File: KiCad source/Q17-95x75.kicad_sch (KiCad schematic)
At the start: 78 parts, among them J1 Input, J2 Terminal, J3 Terminal, Q1 IRF610, Q10 2SA970, Q11 BS250P, Q12 2SC2240 / AC181, Q13 IRF610, Q14 IRF9610, Q15 FQA46N15, Q16 FQA36P15, Q2 2SA970, Q3 2SC2240, Q4 IRF9610, Q5 IRF9610, Q6 IRF610, Q7 2SC2240, Q8 2N7000, Q9 BS250P, U1 OPA1641

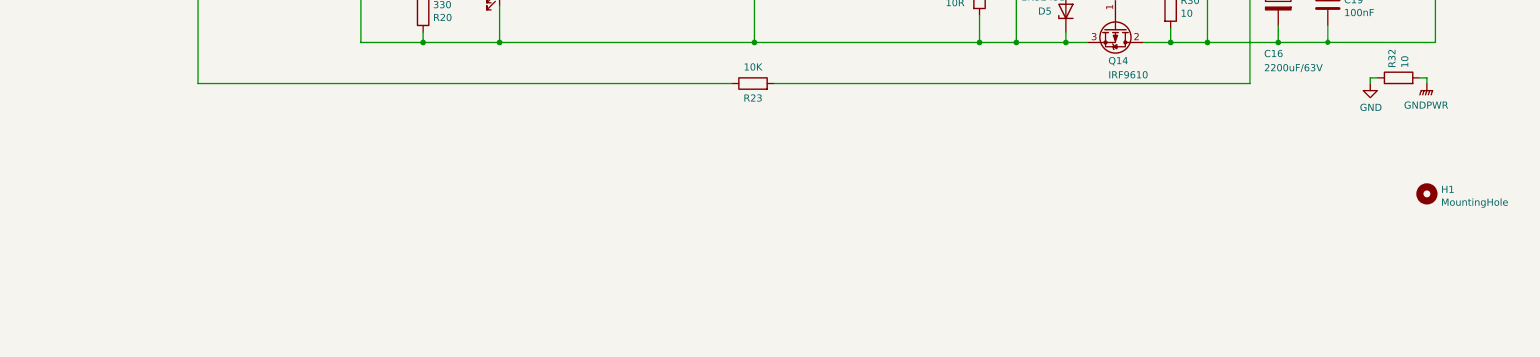
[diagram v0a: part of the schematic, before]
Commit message: General cleanup and parts references added in schematic.
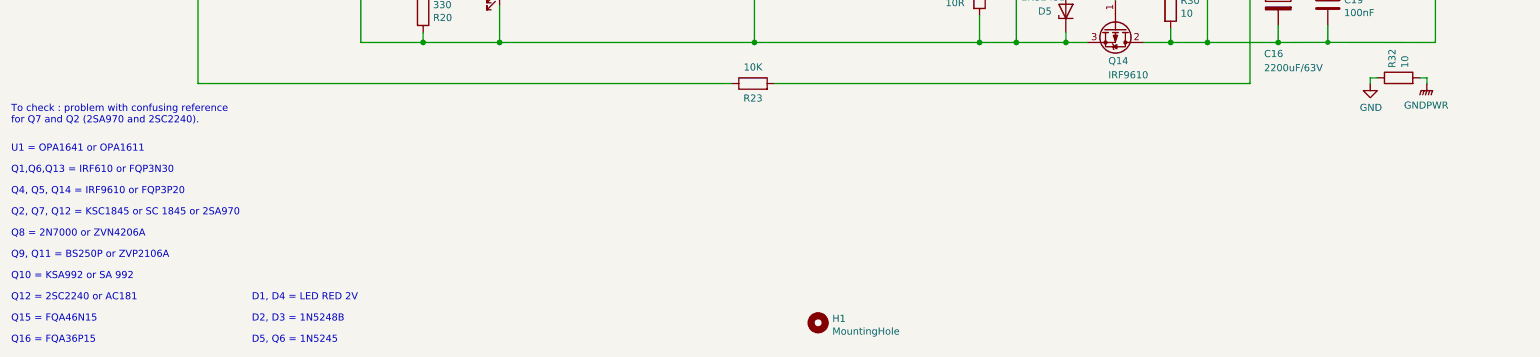
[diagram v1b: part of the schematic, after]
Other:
- note added: "D1, D4 = LED RED 2V"
- note added: "D2, D3 = 1N5248B"
- note added: "D5, Q6 = 1N5245"
- note added: "Q1,Q6,Q13 = IRF610 or FQP3N30"
- note added: "Q10 = KSA992 or SA 992"
- note added: "Q12 = 2SC2240 or AC181"
- note added: "Q15 = FQA46N15"
- note added: "Q16 = FQA36P15"
- note added: "Q2, Q7, Q12 = KSC1845 or SC 1845 or 2SA970"
- note added: "Q4, Q5, Q14 = IRF9610 or FQP3P20"
- note added: "Q8 = 2N7000 or ZVN4206A"
- note added: "Q9, Q11 = BS250P or ZVP2106A"
- note added: "To check : problem with confusing reference for Q7 and Q2 (2SA970 and 2SC2240)."
- note added: "U1 = OPA1641 or OPA1611"
- title: Q17 -> Q17 Amplifier
- moved on the sheet: H1

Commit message: Update diagram for Q17-95x75
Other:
- note added: "C1 and C7 : Use good MKP capacitor."
- note added: "C10 : Use good Mica cacaitor."
- note added: "C6 : Use bipolar capacitor if possible."
- note added: "D1, D4 : LED RED 2V"
- note added: "D2, D3 : 1N5248B"
- note added: "D5, Q6 : 1N5245"
- note added: "L1 : Use 18 turns of 1mm copper insulated wire with a 8mm diameter tube."
- note added: "Q1, Q6, Q13 : IRF610 or FQP3N30"
- note added: "Q10 : KSA992"
- note added: "Q12 : 2SC2240 or AC181"
- note added: "Q15 : FQA46N15"
- note added: "Q16 : FQA36P15"
- note added: "Q2, Q7, Q12 : KSC1845 or 2SA970"
- note added: "Q4, Q5, Q14 : IRF9610 or FQP3P20"
- note added: "Q8 : 2N7000 or ZVN4206AV"
- note added: "Q9, Q11 : BS250P (Diodes Inc) or ZVP2106A"
- note added: "U1 : OPA1641 or OPA1611"
- note removed: "D1, D4 = LED RED 2V"
- note removed: "D2, D3 = 1N5248B"
- note removed: "D5, Q6 = 1N5245"
- note removed: "Q1,Q6,Q13 = IRF610 or FQP3N30"
- note removed: "Q10 = KSA992 or SA 992"
- note removed: "Q12 = 2SC2240 or AC181"
- note removed: "Q15 = FQA46N15"
- note removed: "Q16 = FQA36P15"
- note removed: "Q2, Q7, Q12 = KSC1845 or SC 1845 or 2SA970"
- note removed: "Q4, Q5, Q14 = IRF9610 or FQP3P20"
- note removed: "Q8 = 2N7000 or ZVN4206A"
- note removed: "Q9, Q11 = BS250P or ZVP2106A"
- note removed: "To check : problem with confusing reference for Q7 and Q2 (2SA970 and 2SC2240)."
- note removed: "U1 = OPA1641 or OPA1611"

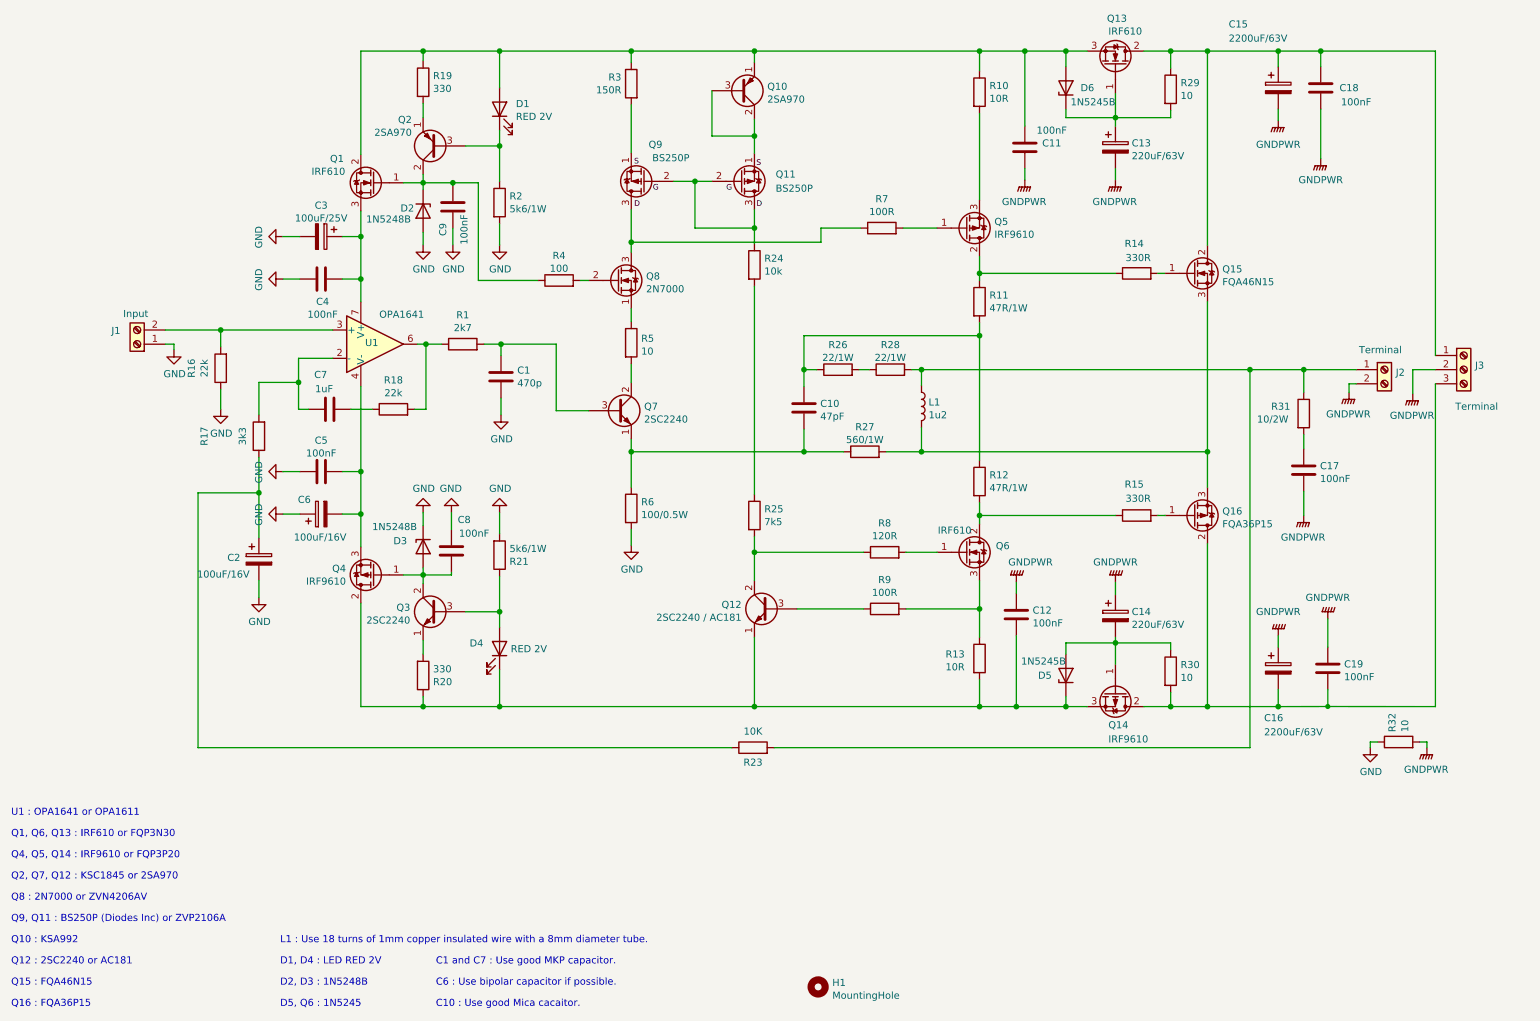
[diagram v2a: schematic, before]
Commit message: Update PCB to 10b12
- Changed footprint for KSC1845 (Q2, Q7 and Q12).
- Updated transistors references on diagram and PCB.
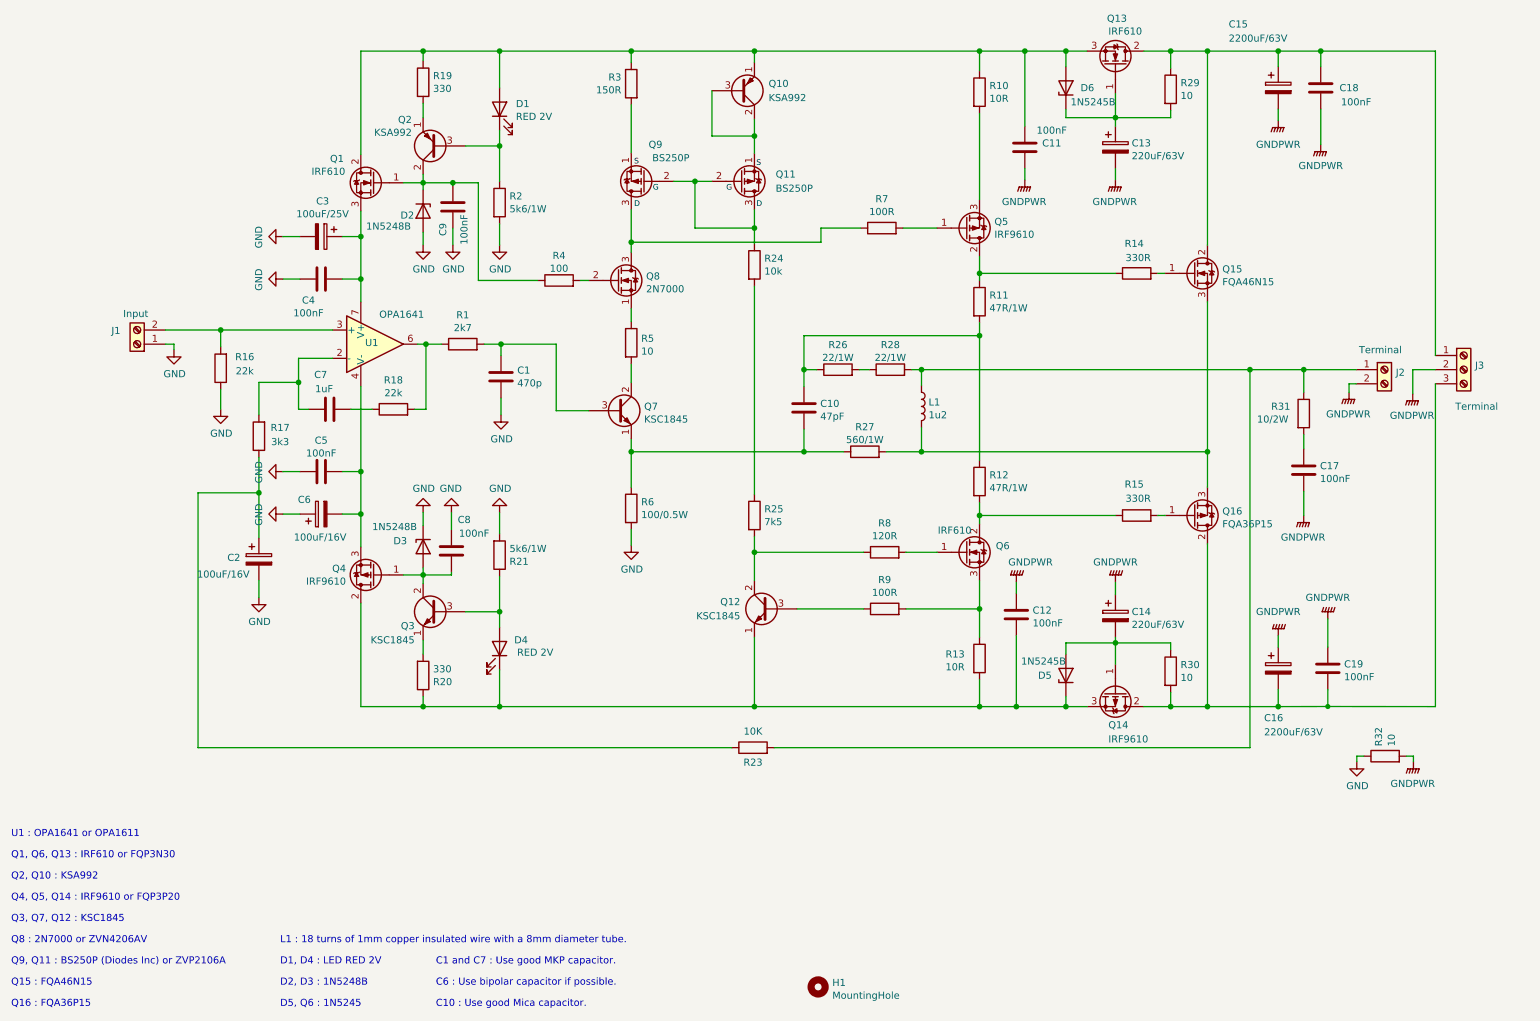
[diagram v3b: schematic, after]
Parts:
- Q10, Q2: value 2SA970 -> KSA992
- Q12: value 2SC2240 / AC181 -> KSC1845
- Q3, Q7: value 2SC2240 -> KSC1845
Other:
- note added: "C10 : Use good Mica capacitor."
- note added: "L1 : 18 turns of 1mm copper insulated wire with a 8mm diameter tube."
- note added: "Q2, Q10 : KSA992"
- note added: "Q3, Q7, Q12 : KSC1845"
- note removed: "C10 : Use good Mica cacaitor."
- note removed: "L1 : Use 18 turns of 1mm copper insulated wire with a 8mm diameter tube."
- note removed: "Q10 : KSA992"
- note removed: "Q12 : 2SC2240 or AC181"
- note removed: "Q2, Q7, Q12 : KSC1845 or 2SA970"
- moved on the sheet: R32

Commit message: Update Diagram and PCB to 1.0b13
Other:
- note added: "C1 and C10 : Use good Mica or Polystyrene capacitor."
- note added: "C7 : Use good MKP capacitor."
- note removed: "C1 and C7 : Use good MKP capacitor."
- note removed: "C10 : Use good Mica capacitor."

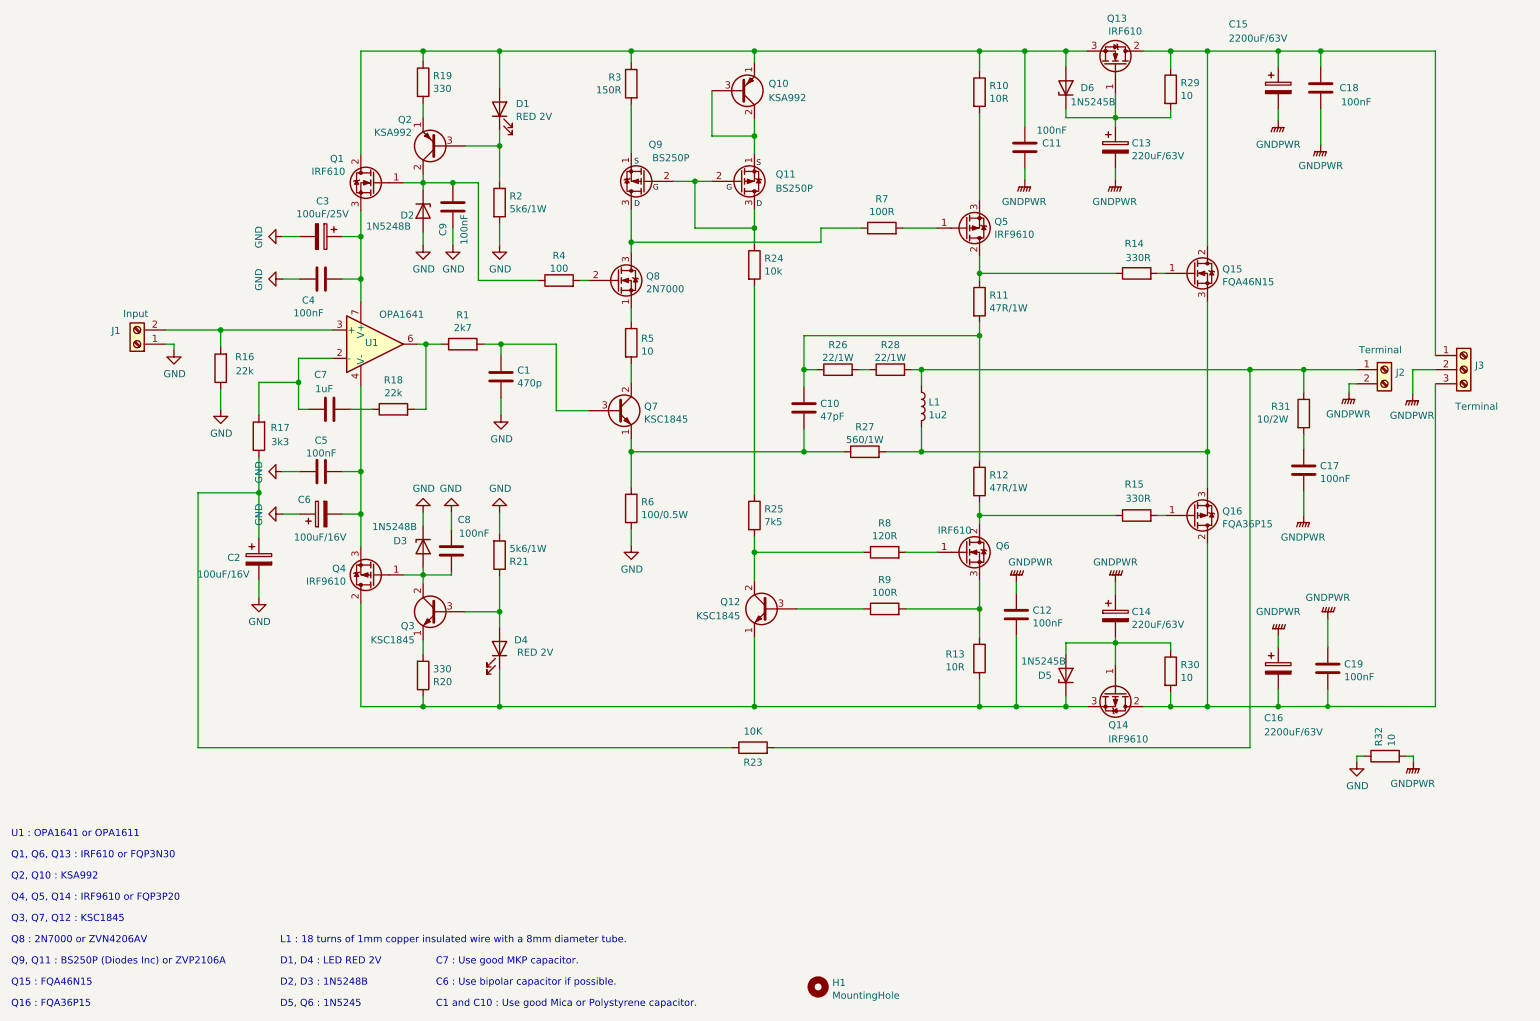
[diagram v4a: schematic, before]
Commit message: PCB and diagram v1.0.b16
- Replaced Q12 by BD139 and TO-126 footprint.
- Optimisation of ground plane.
- Add of missing R2 (yes after 16 beta!!).
- Changed footprint of C7.
- Add some 3D pictures.
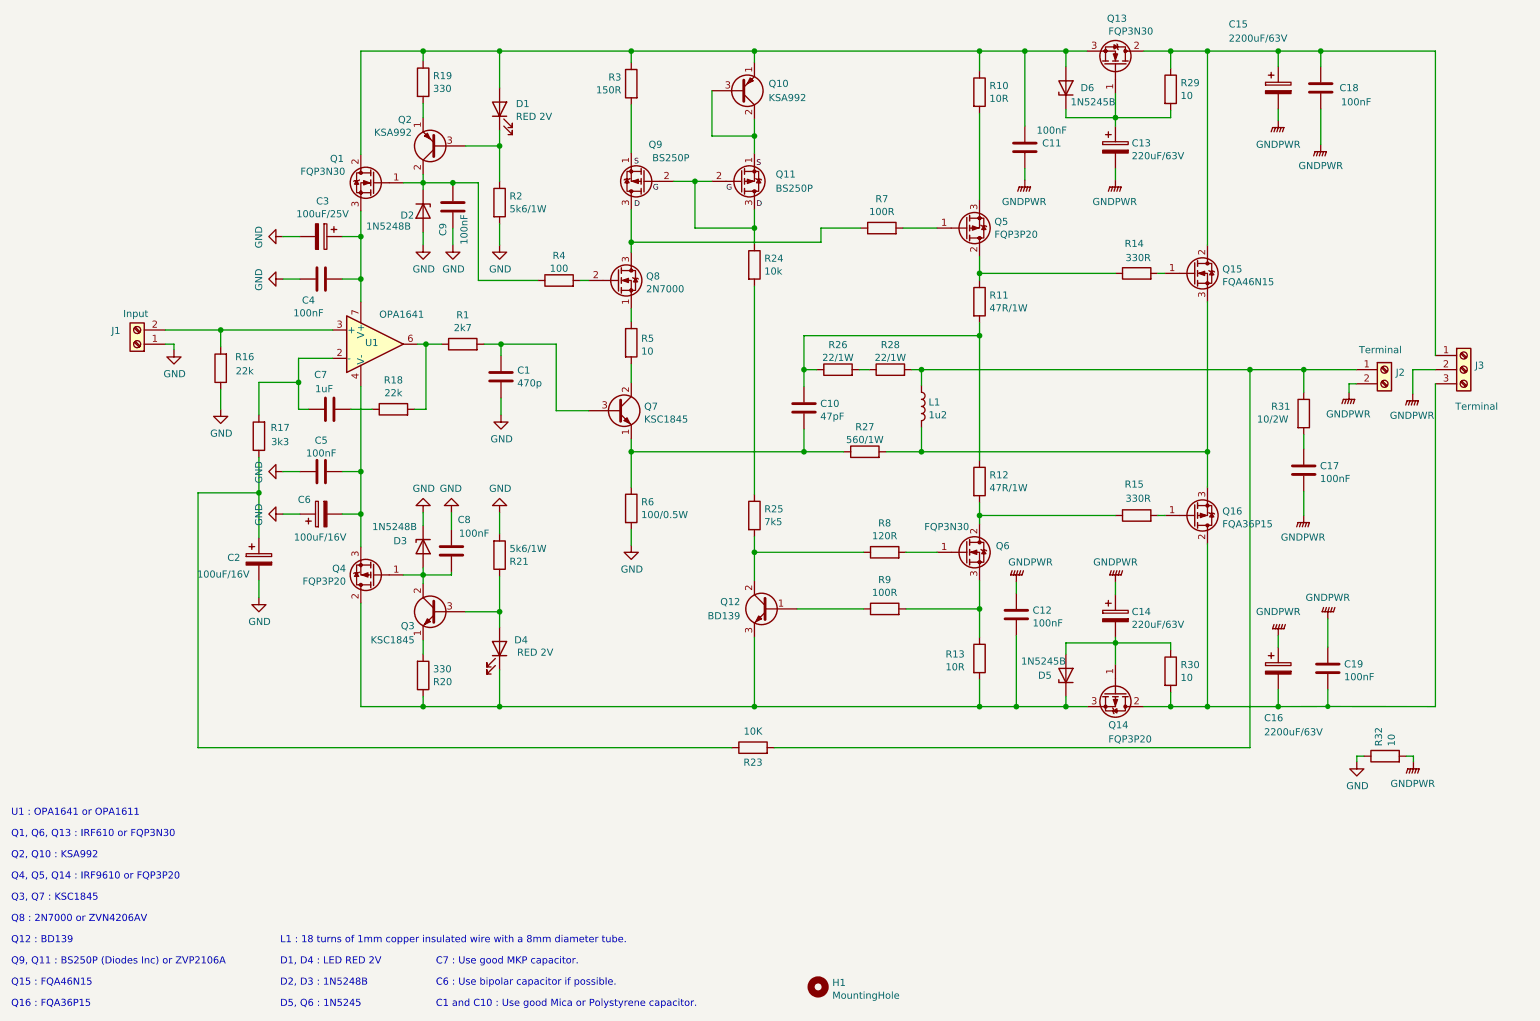
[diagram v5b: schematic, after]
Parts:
- Q1, Q13, Q6: value IRF610 -> FQP3N30
- Q12: value KSC1845 -> BD139; footprint Package_TO_SOT_THT:TO-92 -> Package_TO_SOT_THT:TO-126-3_Vertical; symbol Device:Q_NPN_ECB -> Device:Q_NPN_BCE
- Q14, Q4, Q5: value IRF9610 -> FQP3P20
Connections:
- net at C12.2, D4.1 (K), D5.1 (K)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: now also Q12.3 (E); no longer Q12.1 (E)
- net at R9.1: now also Q12.1 (B); no longer Q12.3 (B)
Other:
- note added: "Q12 : BD139"
- note added: "Q3, Q7 : KSC1845"
- note removed: "Q3, Q7, Q12 : KSC1845"
